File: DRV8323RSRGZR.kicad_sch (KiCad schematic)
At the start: 35 parts, among them CN2 MR60PW-M, Q1 IRF7480MTRPBF, Q2 IRF7480MTRPBF, Q3 IRF7480MTRPBF, Q4 IRF7480MTRPBF, Q5 IRF7480MTRPBF, Q6 IRF7480MTRPBF, U4 AMS1117-3.3, U5 DRV8323RSRGZR

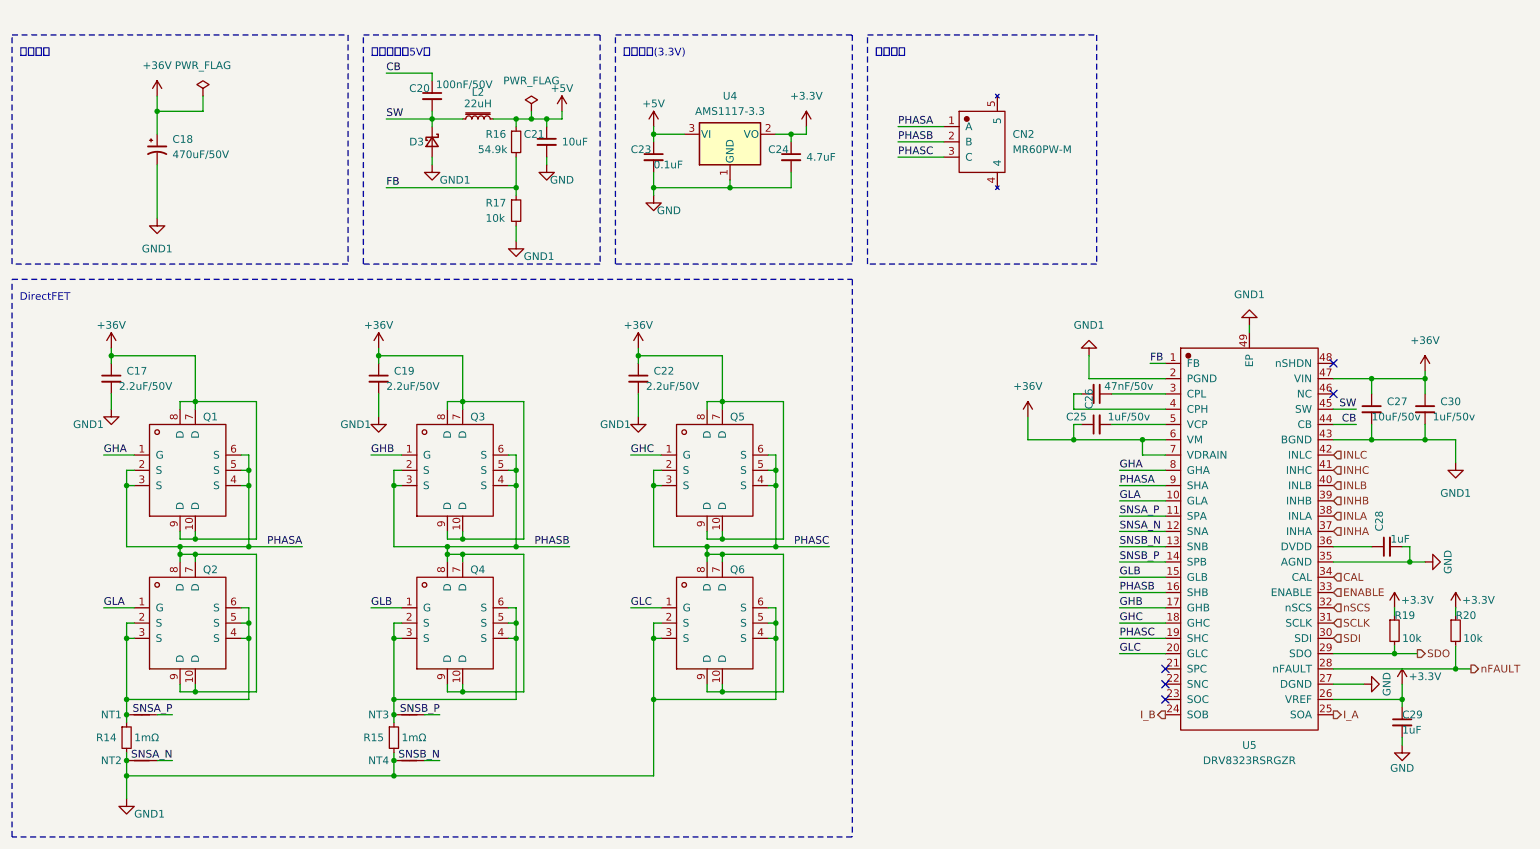
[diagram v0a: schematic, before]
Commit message: 参考MIT驱动器进行改版
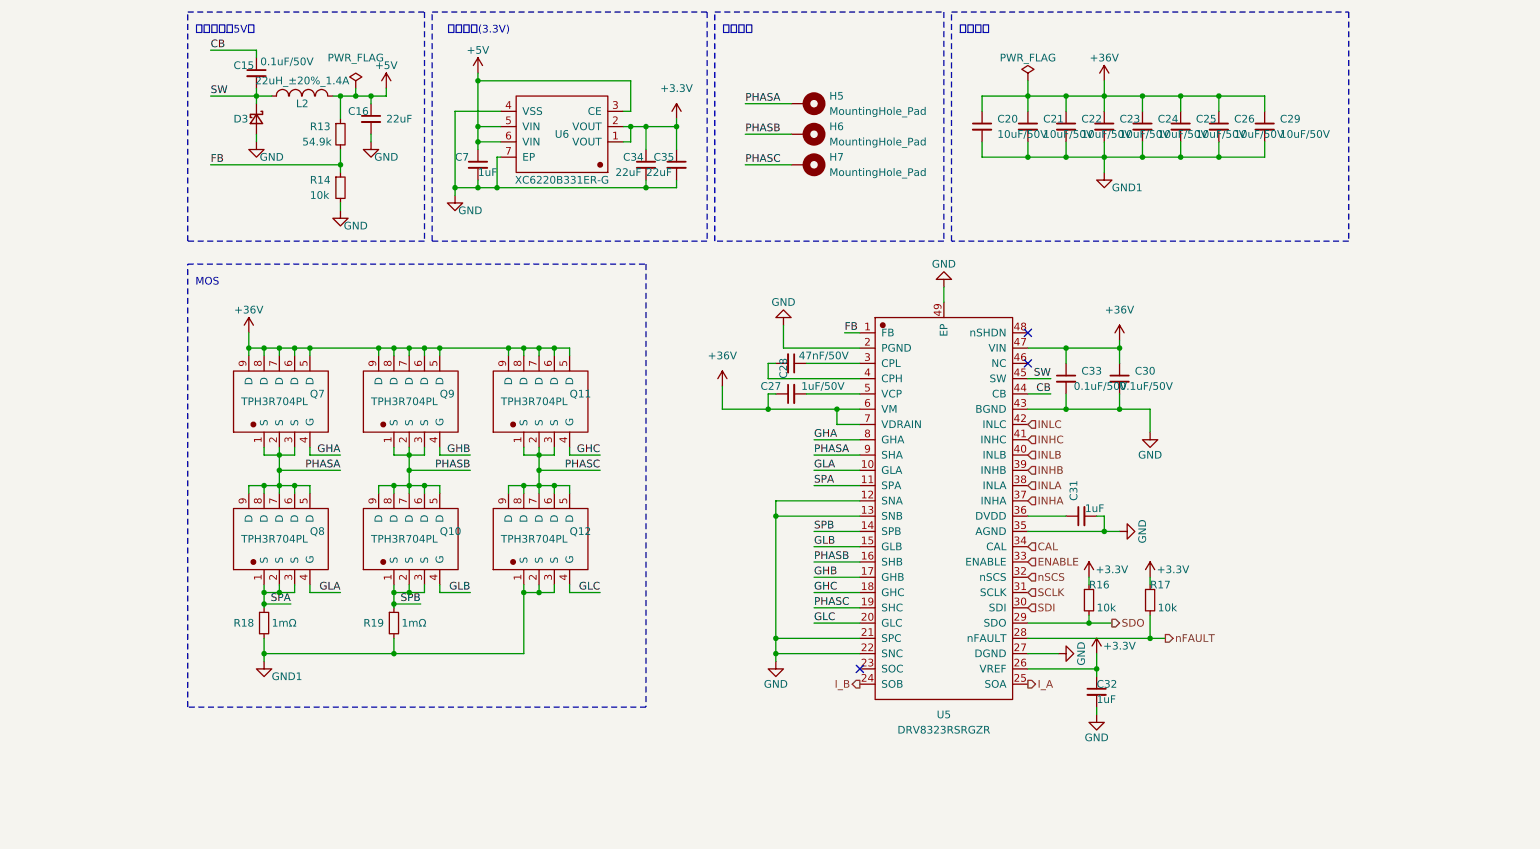
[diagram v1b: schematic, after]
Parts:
- removed C17, C19: 2.2uF/50V, Capacitor_SMD:C_0603_1608Metric_Pad1.08x0.95mm_HandSolder, symbol Device:C_Small
- removed C18: 470uF/50V, Capacitor_SMD:CP_Elec_16x17.5, symbol Device:C_Polarized_Small_US
- removed CN2: MR60PW-M, Rick_Connector:MR60PW-M, symbol Rick_Connector:MR60PW-M
- removed L2: 22uH, Inductor_SMD:L_6.3x6.3_H3, symbol Device:L_Iron_Small
- removed NT1, NT2, NT3, NT4: NetTie_2, NetTie:NetTie-2_SMD_Pad0.5mm, symbol Device:NetTie_2
- removed Q1, Q2, Q3, Q4, Q5, Q6: IRF7480MTRPBF, Rick_MOSFET:IRF7480MTRPBF, symbol Rick_MOSFET:IRF7480MTRPBF
- removed R14, R15: 1mΩ, Resistor_SMD:R_0805_2012Metric_Pad1.20x1.40mm_HandSolder, symbol Device:R_Small
- removed U4: AMS1117-3.3, Rick_Regulator_Linear:AMS1117-3.3, symbol Rick_Regulator_Linear:AMS1117-3.3
- added C20, C21, C25, C26, C29: 10uF/50V, Capacitor_SMD:C_1206_3216Metric_Pad1.33x1.80mm_HandSolder, symbol Device:C_Small
- added C34, C35: 22uF, Capacitor_SMD:C_0603_1608Metric_Pad1.08x0.95mm_HandSolder, symbol Device:C_Small
- added C7: 1uF, Capacitor_SMD:C_0402_1005Metric_Pad0.74x0.62mm_HandSolder, symbol Device:C_Small
- added H5, H6, H7: MountingHole_Pad, CawDrive_Connector:POWER_PAD, symbol Mechanical:MountingHole_Pad
- added L2: 22uH_±20%_1.4A, Rick_Inductor:LQH5BPB220MT0L_IND-SMD_L5.0-W5.0, symbol Rick_Inductor:LQH5BPB220MT0L_22uH_±20%_1.4A
- added Q10, Q11, Q12, Q7, Q8, Q9: TPH3R704PL, Rick_MOSFET:TPHR8504PL,L1Q, symbol Rick_MOSFET:TPH3R704PL
- added R18, R19: 1mΩ, Resistor_SMD:R_1210_3225Metric_Pad1.30x2.65mm_HandSolder, symbol Device:R_Small
- added U6: XC6220B331ER-G, Rick_Regulator_Linear:XC6220B331ER-G_USP-6C_L2.0-W1.8-P0.50-BL-EP, symbol Rick_Regulator_Linear:XC6220B331ER-G
- C15: renamed from C20; value 100nF/50V -> 0.1uF/50V
- C16: renamed from C21; value 10uF -> 22uF
- C22: value 2.2uF/50V -> 10uF/50V; footprint Capacitor_SMD:C_0603_1608Metric_Pad1.08x0.95mm_HandSolder -> Capacitor_SMD:C_1206_3216Metric_Pad1.33x1.80mm_HandSolder
- C23: value 0.1uF -> 10uF/50V; footprint Capacitor_SMD:C_0603_1608Metric_Pad1.08x0.95mm_HandSolder -> Capacitor_SMD:C_1206_3216Metric_Pad1.33x1.80mm_HandSolder
- C24: value 4.7uF -> 10uF/50V; footprint Capacitor_SMD:C_0603_1608Metric_Pad1.08x0.95mm_HandSolder -> Capacitor_SMD:C_1206_3216Metric_Pad1.33x1.80mm_HandSolder
- C27: renamed from C25; value 47nF/50v -> 47nF/50V; footprint Capacitor_SMD:C_0603_1608Metric_Pad1.08x0.95mm_HandSolder -> Capacitor_SMD:C_0402_1005Metric_Pad0.74x0.62mm_HandSolder
- C28: renamed from C26; value 1uF/50v -> 1uF/50V
- C30: renamed from C27; value 10uF/50v -> 0.1uF/50V; footprint Capacitor_SMD:C_0603_1608Metric_Pad1.08x0.95mm_HandSolder -> Capacitor_SMD:C_1206_3216Metric_Pad1.33x1.80mm_HandSolder
- C31: renamed from C28; footprint Capacitor_SMD:C_0603_1608Metric_Pad1.08x0.95mm_HandSolder -> Capacitor_SMD:C_0402_1005Metric_Pad0.74x0.62mm_HandSolder
- C32: renamed from C29; footprint Capacitor_SMD:C_0603_1608Metric_Pad1.08x0.95mm_HandSolder -> Capacitor_SMD:C_0402_1005Metric_Pad0.74x0.62mm_HandSolder
- C33: renamed from C30; value 1uF/50v -> 0.1uF/50V
- D3: footprint Diode_SMD:D_SMA_Handsoldering -> Diode_SMD:D_SOD-123
- R13: renamed from R16; footprint Resistor_SMD:R_0603_1608Metric_Pad0.98x0.95mm_HandSolder -> Resistor_SMD:R_0402_1005Metric_Pad0.72x0.64mm_HandSolder
- R14: renamed from R17; footprint Resistor_SMD:R_0603_1608Metric_Pad0.98x0.95mm_HandSolder -> Resistor_SMD:R_0402_1005Metric_Pad0.72x0.64mm_HandSolder
- R16: renamed from R19; footprint Resistor_SMD:R_0603_1608Metric_Pad0.98x0.95mm_HandSolder -> Resistor_SMD:R_0402_1005Metric_Pad0.72x0.64mm_HandSolder
- R17: renamed from R20; footprint Resistor_SMD:R_0603_1608Metric_Pad0.98x0.95mm_HandSolder -> Resistor_SMD:R_0402_1005Metric_Pad0.72x0.64mm_HandSolder
- U5: footprint Rick_Drive:DRV8323RSRGZR -> Rick_Drive:DRV8323RS_QFN-48-EP(7x7)
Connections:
- net SNSA_N is gone; now on net GND: U5.12 (SNA)
- net SNSB_N is gone; now on net GND: U5.13 (SNB)
- net +3.3V: now also C34.1, C35.1, U6.1 (VOUT), U6.2 (VOUT); no longer C24.1
- net +36V: now also C23.1, C24.1, C20.1, C21.1, C25.1, C26.1, C29.1, Q11.5 (D), Q11.6 (D), Q11.7 (D), Q11.8 (D), Q11.9 (D), Q7.5 (D), Q7.6 (D), Q7.7 (D), Q7.8 (D), Q7.9 (D), Q9.5 (D), Q9.6 (D), Q9.7 (D), Q9.8 (D), Q9.9 (D)
- net +5V: now also C7.1, L2.2, U6.3 (CE), U6.5 (VIN), U6.6 (VIN); no longer C23.1
- net GHA: now also Q7.4 (G)
- net GHB: now also Q9.4 (G)
- net GHC: now also Q11.4 (G)
- net GLA: now also Q8.4 (G)
- net GLB: now also Q10.4 (G)
- net GLC: now also Q12.4 (G)
- net GND: now also C30.2, C33.2, D3.2 (A), R14.2, U5.2 (PGND), U5.21 (SPC), U5.22 (SNC), U5.43 (BGND), U5.49 (EP), C34.2, C35.2, C7.2, U6.4 (VSS), U6.7 (EP); no longer C23.2, C24.2
- net GND1: now also C23.2, C24.2, C20.2, C21.2, C25.2, C26.2, C29.2, Q12.1 (S), Q12.2 (S), Q12.3 (S), R18.2, R19.2; no longer C30.2, C33.2, D3.2 (A), R14.2, U5.2 (PGND), U5.43 (BGND), U5.49 (EP)
- net PHASA: now also H5.1, Q7.1 (S), Q7.2 (S), Q7.3 (S), Q8.5 (D), Q8.6 (D), Q8.7 (D), Q8.8 (D), Q8.9 (D)
- net PHASB: now also H6.1, Q10.5 (D), Q10.6 (D), Q10.7 (D), Q10.8 (D), Q10.9 (D), Q9.1 (S), Q9.2 (S), Q9.3 (S)
- net PHASC: now also H7.1, Q11.1 (S), Q11.2 (S), Q11.3 (S), Q12.5 (D), Q12.6 (D), Q12.7 (D), Q12.8 (D), Q12.9 (D)
- net SW: now also L2.1
- net SNSA_P renamed SPA
- net SPA: now also Q8.1 (S), Q8.2 (S), Q8.3 (S), R18.1
- net SNSB_P renamed SPB
- net SPB: now also Q10.1 (S), Q10.2 (S), Q10.3 (S), R19.1
- no-connect marks 5 -> 3
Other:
- note added: "MOS"
- note added: "滤波电容"
- note removed: "DirectFET"
- note removed: "电源滤波"
- moved on the sheet: C15, C16, C27, C28, C30, C31, C32, C33, D3, R13, R14, R16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

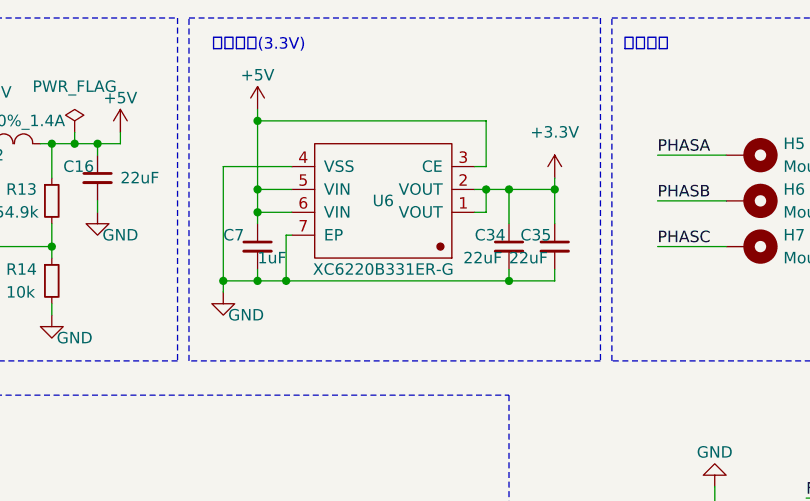
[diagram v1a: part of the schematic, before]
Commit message: 将线性稳压芯片和CAN芯片替换成TI的相关型号
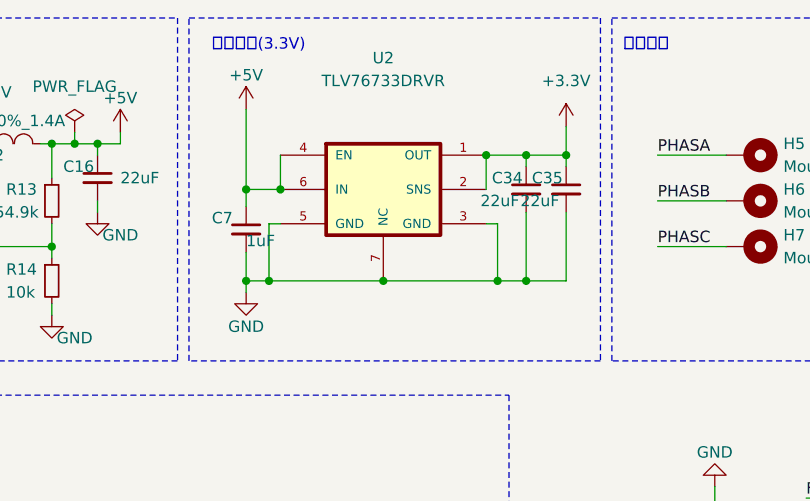
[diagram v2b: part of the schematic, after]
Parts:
- removed U6: XC6220B331ER-G, Rick_Regulator_Linear:XC6220B331ER-G_USP-6C_L2.0-W1.8-P0.50-BL-EP, symbol Rick_Regulator_Linear:XC6220B331ER-G
- added U2: TLV76733DRVR, Rick_Regulator_Linear:TLV76733DRVR_SON65P200X200X80-7N, symbol Rick_Regulator_Linear:TLV76733DRVR
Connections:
- net +3.3V: now also U2.1 (OUT), U2.2 (SNS)
- net +5V: now also U2.4 (EN), U2.6 (IN)
- net GND: now also U2.3 (GND), U2.5 (GND), U2.7 (NC)
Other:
- moved on the sheet: C34, C35, C7

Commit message: 优化布线
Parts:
- added C10: 0.1uF/50V, Capacitor_SMD:C_0402_1005Metric_Pad0.74x0.62mm_HandSolder, symbol Device:C_Small
- R13: value 54.9k -> 54.9k ±0.1%
- R14: value 10k -> 10k ±0.1%
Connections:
- net +36V: now also C10.1
- net GND: no longer U5.12 (SNA), U5.13 (SNB), U5.21 (SPC), U5.22 (SNC)
- net GND1: now also U5.12 (SNA), U5.13 (SNB), U5.21 (SPC), U5.22 (SNC), C10.2
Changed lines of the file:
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@@
   (junction (at 205.74 97.79) (diameter 0) (color 0 0 0 0)
+  )
+  (junction (at 148.59 140.97) (diameter 0) (color 0 0 0 0)
   )
   (junction (at 106.68 87.63) (diameter 0) (color 0 0 0 0)
@@
     (stroke (width 0) (type default))
   )
+  (wire (pts (xy 232.41 77.47) (xy 232.41 78.74))
+    (stroke (width 0) (type default))
+  )
   (wire (pts (xy 100.33 60.96) (xy 113.03 60.96))
     (stroke (width 0) (type default))
@@
     (stroke (width 0) (type default))
   )
+  (wire (pts (xy 232.41 83.82) (xy 232.41 85.09))
+    (stroke (width 0) (type default))
+  )
   (wire (pts (xy 133.35 53.34) (xy 133.35 60.96))
     (stroke (width 0) (type default))
@@
     (stroke (width 0) (type default))
   )
+  (wire (pts (xy 148.59 140.97) (xy 148.59 142.24))
+    (stroke (width 0) (type default))
+  )
   (wire (pts (xy 209.55 45.72) (xy 209.55 48.26))
     (stroke (width 0) (type default))
@@
     (stroke (width 0) (type default))
   )
-  (wire (pts (xy 148.59 138.43) (xy 148.59 139.7))
+  (wire (pts (xy 148.59 138.43) (xy 148.59 140.97))
     (stroke (width 0) (type default))
   )
@@
   )
   (wire (pts (xy 60.96 110.49) (xy 63.5 110.49))
+    (stroke (width 0) (type default))
+  )
+  (wire (pts (xy 147.32 140.97) (xy 148.59 140.97))
     (stroke (width 0) (type default))
   )
@@
     (fill (type none))
   )
-  (rectangle (start 177.8 31.75) (end 243.84 69.85)
+  (rectangle (start 177.8 31.75) (end 243.205 69.85)
     (stroke (width 0) (type dash))
     (fill (type none))
@@
         (path "/80524a83-b783-469c-b956-da06086e2ffd/e4f6c5bf-0795-4b0d-aae9-e947b60f2c3b"
           (reference "C23") (unit 1)
-        )
-      )
-    )
-  )
-  (symbol (lib_id "power:GND") (at 148.59 139.7 0) (unit 1)
-    (in_bom yes) (on_board yes) (dnp no)
-    (property "Reference" "#PWR058" (at 148.59 146.05 0)
-      (effects (font (size 1.27 1.27)) hide)
-    )
-    (property "Value" "GND" (at 148.59 143.51 0)
-      (effects (font (size 1.27 1.27)))
-    )
-    (property "Footprint" "" (at 148.59 139.7 0)
-      (effects (font (size 1.27 1.27)) hide)
-    )
-    (property "Datasheet" "" (at 148.59 139.7 0)
-      (effects (font (size 1.27 1.27)) hide)
-    )
-    (pin "1")
-    (instances
-      (project "CawDrive"
-        (path "/80524a83-b783-469c-b956-da06086e2ffd/e4f6c5bf-0795-4b0d-aae9-e947b60f2c3b"
-          (reference "#PWR058") (unit 1)
         )
       )
@@
     )
   )
+  (symbol (lib_id "power:GND1") (at 148.59 142.24 0) (unit 1)
+    (in_bom yes) (on_board yes) (dnp no)
+    (property "Reference" "#PWR023" (at 148.59 148.59 0)
+      (effects (font (size 1.27 1.27)) hide)
+    )
+    (property "Value" "GND1" (at 152.4 144.78 0)
+      (effects (font (size 1.27 1.27)))
+    )
+    (property "Footprint" "" (at 148.59 142.24 0)
+      (effects (font (size 1.27 1.27)) hide)
+    )
+    (property "Datasheet" "" (at 148.59 142.24 0)
+      (effects (font (size 1.27 1.27)) hide)
+    )
+    (pin "1")
+    (instances
+      (project "CawDrive"
+        (path "/80524a83-b783-469c-b956-da06086e2ffd/e4f6c5bf-0795-4b0d-aae9-e947b60f2c3b"
+          (reference "#PWR023") (unit 1)
+        )
+      )
+    )
+  )
   (symbol (lib_id "Device:C_Small") (at 128.905 50.8 0) (unit 1)
     (in_bom yes) (on_board yes) (dnp no)
@@
       (effects (font (size 1.27 1.27)) (justify left))
     )
-    (property "Value" "10k" (at 71.12 62.23 0)
+    (property "Value" "10k ±0.1%" (at 64.135 61.595 0)
       (effects (font (size 1.27 1.27)) (justify left))
     )
@@
     )
   )
+  (symbol (lib_id "Device:C_Small") (at 232.41 81.28 0) (unit 1)
+    (in_bom yes) (on_board yes) (dnp no) (fields_autoplaced)
+    (property "Reference" "C10" (at 235.585 80.0163 0)
+      (effects (font (size 1.27 1.27)) (justify left))
+    )
+    (property "Value" "0.1uF/50V" (at 235.585 82.5563 0)
+      (effects (font (size 1.27 1.27)) (justify left))
+    )
+    (property "Footprint" "Capacitor_SMD:C_0402_1005Metric_Pad0.74x0.62mm_HandSolder" (at 232.41 81.28 0)
+      (effects (font (size 1.27 1.27)) hide)
+    )
+    (property "Datasheet" "~" (at 232.41 81.28 0)
+      (effects (font (size 1.27 1.27)) hide)
+    )
+    (pin "1")
+    (pin "2")
+    (instances
+      (project "CawDrive"
+        (path "/80524a83-b783-469c-b956-da06086e2ffd/e4f6c5bf-0795-4b0d-aae9-e947b60f2c3b"
+          (reference "C10") (unit 1)
+        )
+      )
+    )
+  )
   (symbol (lib_id "Device:R_Small") (at 63.5 133.35 0) (unit 1)
     (in_bom yes) (on_board yes) (dnp no)
@@
         (path "/80524a83-b783-469c-b956-da06086e2ffd/e4f6c5bf-0795-4b0d-aae9-e947b60f2c3b"
           (reference "C16") (unit 1)
+        )
+      )
+    )
+  )
+  (symbol (lib_id "power:PWR_FLAG") (at 147.32 140.97 90) (unit 1)
+    (in_bom yes) (on_board yes) (dnp no)
+    (property "Reference" "#FLG03" (at 145.415 140.97 0)
+      (effects (font (size 1.27 1.27)) hide)
+    )
+    (property "Value" "PWR_FLAG" (at 143.51 140.97 0)
+      (effects (font (size 1.27 1.27)))
+    )
+    (property "Footprint" "" (at 147.32 140.97 0)
+      (effects (font (size 1.27 1.27)) hide)
+    )
+    (property "Datasheet" "~" (at 147.32 140.97 0)
+      (effects (font (size 1.27 1.27)) hide)
+    )
+    (pin "1")
+    (instances
+      (project "CawDrive"
+        (path "/80524a83-b783-469c-b956-da06086e2ffd/e4f6c5bf-0795-4b0d-aae9-e947b60f2c3b"
+          (reference "#FLG03") (unit 1)
         )
       )
@@
     )
   )
+  (symbol (lib_id "power:GND1") (at 232.41 85.09 0) (unit 1)
+    (in_bom yes) (on_board yes) (dnp no)
+    (property "Reference" "#PWR030" (at 232.41 91.44 0)
+      (effects (font (size 1.27 1.27)) hide)
+    )
+    (property "Value" "GND1" (at 236.22 87.63 0)
+      (effects (font (size 1.27 1.27)))
+    )
+    (property "Footprint" "" (at 232.41 85.09 0)
+      (effects (font (size 1.27 1.27)) hide)
+    )
+    (property "Datasheet" "" (at 232.41 85.09 0)
+      (effects (font (size 1.27 1.27)) hide)
+    )
+    (pin "1")
+    (instances
+      (project "CawDrive"
+        (path "/80524a83-b783-469c-b956-da06086e2ffd/e4f6c5bf-0795-4b0d-aae9-e947b60f2c3b"
+          (reference "#PWR030") (unit 1)
+        )
+      )
+    )
+  )
   (symbol (lib_id "Rick_MOSFET:TPH3R704PL") (at 110.49 96.52 90) (unit 1)
     (in_bom yes) (on_board yes) (dnp no)
@@
       (effects (font (size 1.27 1.27)) (justify left))
     )
-    (property "Value" "54.9k" (at 69.85 53.34 0)
+    (property "Value" "54.9k ±0.1%" (at 63.5 53.34 0)
       (effects (font (size 1.27 1.27)) (justify left))
     )
@@
         )
       )
+    )
+  )
+  (symbol (lib_id "power:+36V") (at 232.41 77.47 0) (unit 1)
+    (in_bom yes) (on_board yes) (dnp no)
+    (property "Reference" "#PWR027" (at 232.41 81.28 0)
+      (effects (font (size 1.27 1.27)) hide)
+    )
+    (property "Value" "+36V" (at 232.41 73.66 0)
+      (effects (font (size 1.27 1.27)))
+    )
+    (property "Footprint" "" (at 232.41 77.47 0)
+      (effects (font (size 1.27 1.27)) hide)
+    )
+    (property "Datasheet" "" (at 232.41 77.47 0)
+      (effects (font (size 1.27 1.27)) hide)
+    )
+    (pin "1")
+    (instances
+      (project "CawDrive"
+        (path "/80524a83-b783-469c-b956-da06086e2ffd/e4f6c5bf-0795-4b0d-aae9-e947b60f2c3b"
+          (reference "#PWR027") (unit 1)
+        )
+      )
